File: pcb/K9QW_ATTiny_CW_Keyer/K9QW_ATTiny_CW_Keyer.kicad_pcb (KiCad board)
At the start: 2 copper layers, 50.8 x 31.8 mm, 37 parts, among them J1 Power Input, J2 AudioJack4, J3 AudioJack4, J4 Sidetone, J5 Mounting Hole, Q1 AO3401A, Q2 MMBT2222A, Q3 MMBT3904, Q4 MMBT3904, SW1 Power Switch, SW2 Command, U1 ATtiny85-20P, U2 LD1117S33TR_SOT223

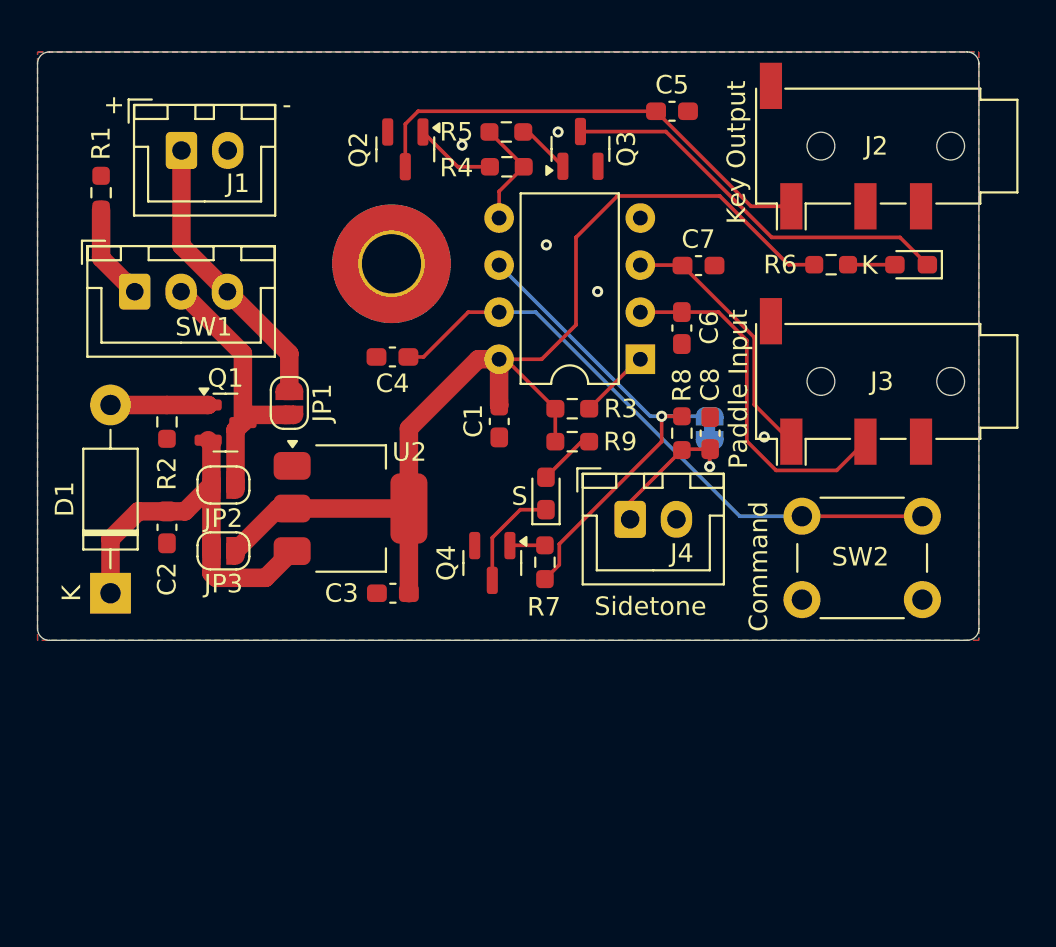
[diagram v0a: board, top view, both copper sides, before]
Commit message: Adding power supply filter cap and preparing buzzer
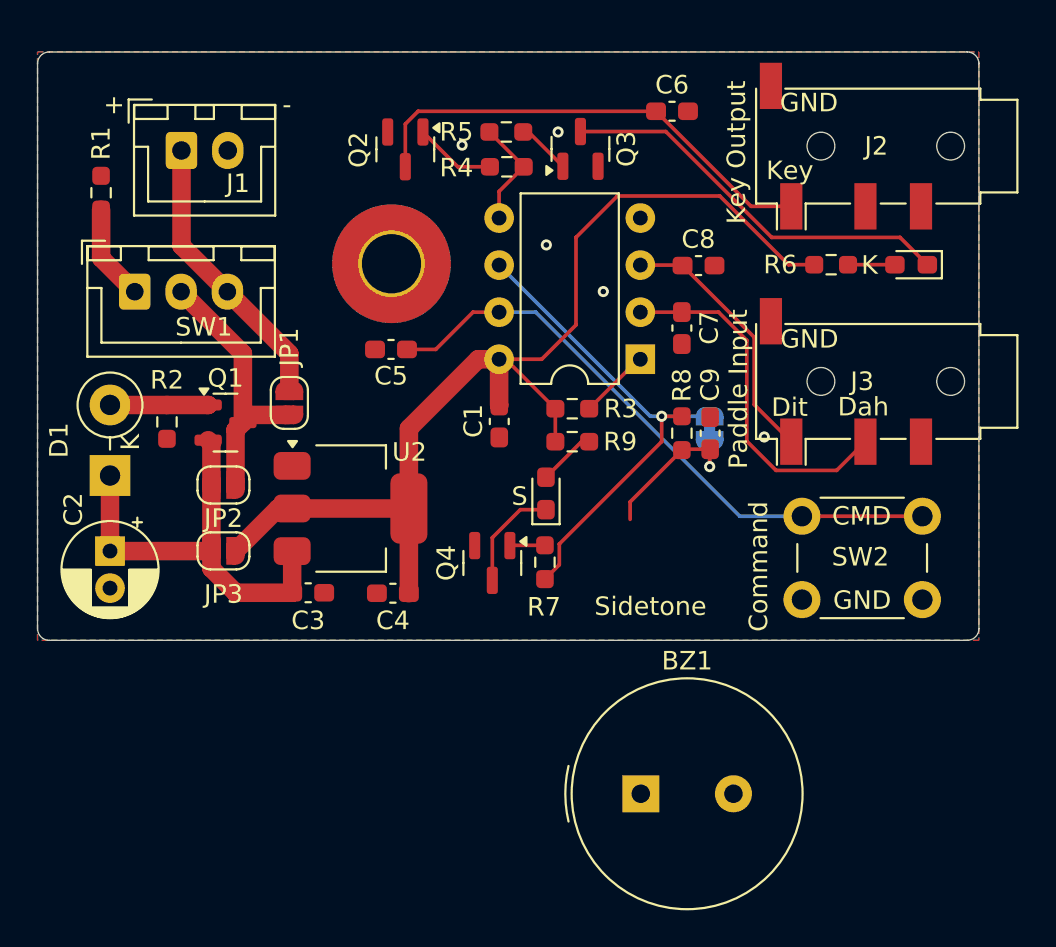
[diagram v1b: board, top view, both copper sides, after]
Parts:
- removed J4: Sidetone, Connector_JST:JST_XH_B2B-XH-A_1x02_P2.50mm_Vertical
- added BZ1: Buzzer, Buzzer_Beeper:Buzzer_TDK_PS1240P02BT_D12.2mm_H6.5mm, F.Cu at (159.0, 126.1)
- added C2: 10uF, Capacitor_THT:CP_Radial_D5.0mm_P2.00mm, F.Cu at (130.4, 113.0)
- D1: footprint Diode_THT:D_DO-41_SOD81_P10.16mm_Horizontal -> Diode_THT:D_DO-41_SOD81_P3.81mm_Vertical_KathodeUp
- D2: value Key -> Key LED
- D3: value Sidetone -> Sidetone LED
- R1: value 50 -> 1k
- R6, R9: value 220 -> 220R
- R8: value 8.2 -> 8.2R
- moved C3 8.40 mm to (141.1, 115.3), turned to 0 degrees
- moved D1 6.35 mm to (130.4, 109.0)
- moved C5 0.41 mm to (145.6, 102.2)
- renumbered C2 to C3, C3 to C4, C4 to C5, C5 to C6, C6 to C7, C7 to C8, C8 to C9
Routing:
- net Net-(D1-K): track 22.8 -> 24.6 mm
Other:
- board text added: "CMD"
- board text added: "Dah"
- board text added: "Dit"
- board text added: "GND"
- board text added: "Key"

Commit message: Laying out buzzer and moving power regulator to back of board
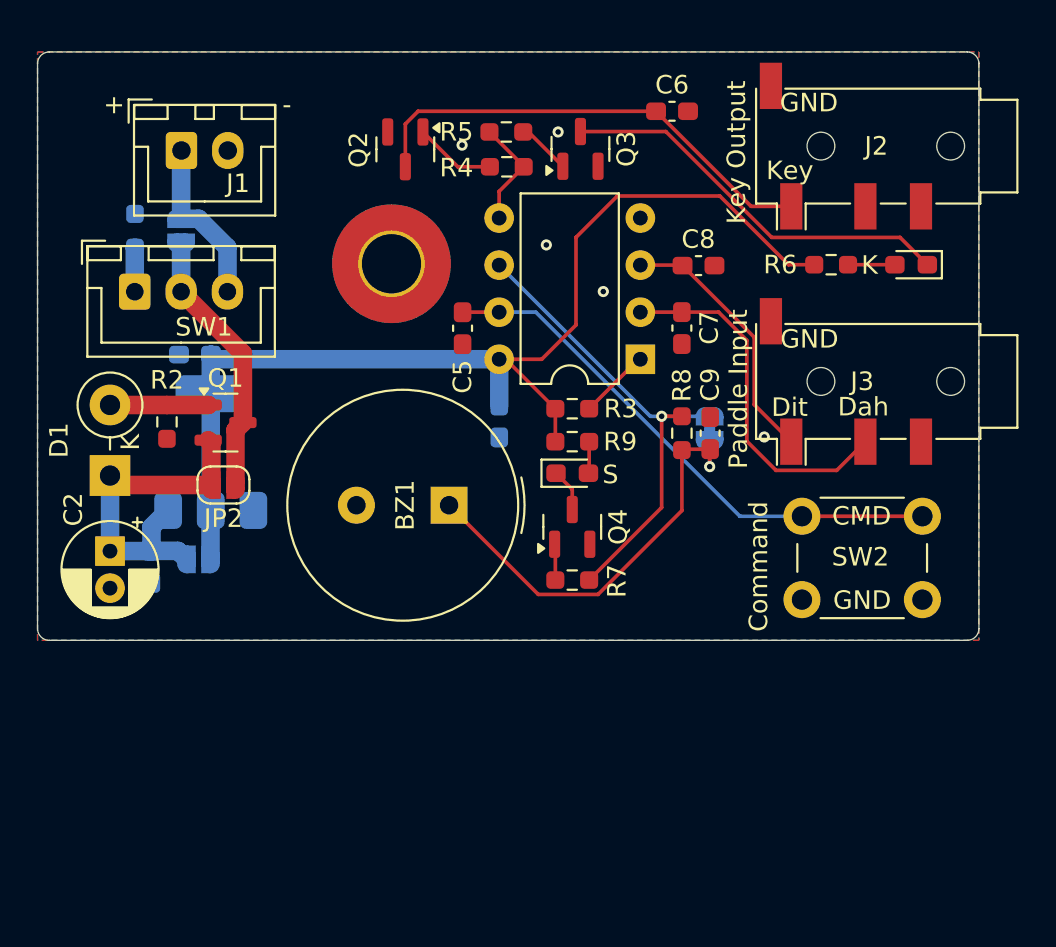
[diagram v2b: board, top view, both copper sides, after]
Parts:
- C1, C3, C4, JP1, JP3, R1, U2: moved to B.Cu
- moved BZ1 18.7 mm to (148.7, 110.6), turned to 180 degrees
- moved C4 16.7 mm to (135.0, 102.4)
- moved JP1 11.0 mm to (134.2, 95.8)
- moved C3 8.57 mm to (132.6, 113.9), turned to -90 degrees
- moved U2 8.14 mm to (135.8, 107.7), turned to 90 degrees
- moved Q4 4.73 mm to (155.3, 111.7), turned to 90 degrees
- moved C5 4.03 mm to (149.4, 101.0), turned to -90 degrees
- moved R1 2.75 mm to (131.7, 95.8)
- moved D3 1.79 mm to (155.3, 108.8), turned to 0 degrees
- moved R7 1.76 mm to (155.3, 114.6), turned to 180 degrees
- moved JP3 1.42 mm to (135.2, 113.5)
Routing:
- net Net-(BZ1-+): track 8.81 -> 23.6 mm
- net VDC: track 15.4 -> 9.22 mm
- net Net-(D1-K): track 24.6 -> 19.1 mm
- net COMMAND: track 33.2 -> 29.4 mm
- net Net-(D3-K): track 5.82 -> 2.32 mm
- net Net-(SW1-A): track 5.18 -> 2.38 mm
- net Net-(D3-A): track 3.12 -> 1.72 mm
- net VCC: track 59.2 -> 60.3 mm
- net SIDETONE: track 27.2 -> 26.3 mm
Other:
- board text removed: "Sidetone"

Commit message: Refining routing
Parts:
- JP4: moved to F.Cu
- moved C9 11.9 mm to (155.2, 115.8), turned to 0 degrees
- moved JP4 10.5 mm to (155.2, 113.7), turned to 0 degrees
- moved R8 7.83 mm to (155.2, 111.7), turned to 180 degrees
- moved Q4 6.52 mm to (161.0, 108.5), turned to 180 degrees
- moved R7 4.52 mm to (155.2, 110.1), turned to 0 degrees
- moved D3 0.35 mm to (155.2, 108.5)
- moved R9 0.24 mm to (155.2, 106.9)
- moved BZ1 0.23 mm to (148.5, 110.6)
- moved R3 0.13 mm to (155.2, 105.4)
- renumbered J5 to J4
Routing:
- net Net-(BZ1-+): track 23.6 -> 13.9 mm, vias 1 -> 0
- net Net-(Q4-B): track 1.95 -> 6.08 mm
- net Net-(D3-K): track 2.32 -> 6.37 mm
- net SIDETONE: track 26.3 -> 22.3 mm, vias 1 -> 0
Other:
- board text added: "Sidetone"

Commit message: Minor
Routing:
- net GND: vias 5 -> 6
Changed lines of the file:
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@@
 		)
 		(fp_text user "K"
-			(at 1.8 1.1 90)
+			(at 1.5748 1.016 90)
 			(layer "F.SilkS")
 			(effects
@@
 		(tags "resistor handsolder")
 		(property "Reference" "R1"
-			(at 2.667 0 90)
+			(at 0 -1.3462 90)
 			(layer "B.SilkS")
 			(effects
@@
 		(tags "solder jumper open")
 		(property "Reference" "JP1"
-			(at 3.0122 0 90)
+			(at 0 1.7526 90)
 			(layer "B.SilkS")
 			(effects
@@
 		(size 0.6)
 		(drill 0.3)
+		(layers "F.Cu" "B.Cu")
+		(free yes)
+		(net 2)
+	)
+	(via
+		(at 150.0886 104.4448)
+		(size 0.6)
+		(drill 0.3)

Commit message: Minor
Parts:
- moved BZ1 3.57 mm to (145.8, 112.9), turned to 90 degrees
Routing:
- net Net-(BZ1-+): track 13.9 -> 15.1 mm
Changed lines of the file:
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@@
 	(footprint "Buzzer_Beeper:Buzzer_TDK_PS1240P02BT_D12.2mm_H6.5mm"
 		(layer "F.Cu")
-		(at 148.471585 110.5662 180)
+		(at 145.796 112.9284 90)
 		(descr "Buzzer, D12.2mm height 6.5mm, https://product.tdk.com/info/en/catalog/datasheets/piezoelectronic_buzzer_ps_en.pdf")
 		(tags "buzzer")
 		(property "Reference" "BZ1"
-			(at 2.548585 -1.9812 180)
+			(at 2.5 0 90)
 			(layer "F.SilkS")
 			(effects
@@
 		)
 		(property "Value" "Buzzer"
-			(at 2.5 7.31 360)
+			(at 2.5 7.31 90)
 			(layer "F.Fab")
 			(effects
@@
 		)
 		(property "Footprint" "Buzzer_Beeper:Buzzer_TDK_PS1240P02BT_D12.2mm_H6.5mm"
-			(at 0 0 180)
+			(at 0 0 90)
 			(unlocked yes)
 			(layer "F.Fab")
@@
 		)
 		(property "Datasheet" ""
-			(at 0 0 180)
+			(at 0 0 90)
 			(unlocked yes)
 			(layer "F.Fab")
@@
 		)
 		(property "Description" "Buzzer, polarized"
-			(at 0 0 180)
+			(at 0 0 90)
 			(unlocked yes)
 			(layer "F.Fab")
@@
 		)
 		(fp_text user "${REFERENCE}"
-			(at 2.5 -2.43 360)
+			(at 2.5 -2.43 90)
 			(layer "F.Fab")
 			(effects
@@
 		)
 		(pad "1" thru_hole rect
-			(at 0 0 180)
+			(at 0 0 90)
 			(size 2 2)
 			(drill 1)
@@
 		)
 		(pad "2" thru_hole circle
-			(at 5 0 180)
+			(at 5 0 90)
 			(size 2 2)
 			(drill 1)
@@
 	)
 	(gr_text "Sidetone"
-		(at 141.2494 108.966 0)
+		(at 144.2466 115.2652 90)
 		(layer "F.SilkS")
 		(effects
@@
 	)
 	(segment
-		(start 149.2261 110.5662)
-		(end 148.700185 110.5662)
-		(width 0.2)
-		(layer "F.Cu")
-		(net 25)
-	)
-	(segment
 		(start 155.8694 114.3115)
 		(end 155.8694 113.7412)
@@
 	(segment
 		(start 154.3569 115.824)
-		(end 153.729385 115.824)
+		(end 148.505215 115.824)
 		(width 0.2)
 		(layer "F.Cu")
@@
 	)
 	(segment
-		(start 155.8694 111.9209)
-		(end 156.1319 111.6584)
+		(start 148.505215 115.824)
+		(end 145.7198 113.038585)
 		(width 0.2)
 		(layer "F.Cu")
@@
 	)
 	(segment
-		(start 153.729385 115.824)
-		(end 148.471585 110.5662)
+		(start 155.8694 111.9209)
+		(end 156.1319 111.6584)
 		(width 0.2)
 		(layer "F.Cu")

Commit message: Minor
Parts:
- moved C1 0.13 mm to (151.4, 105.9)
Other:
- board text added: "ATTiny85 CW Keyer - Rev 0 PCB by Edward Sandor, K9QW 2024-08"
- board text removed: "ATTiny85 CW Keyer PCB by Edward Sandor, K9QW Sandor Laboratories 2024-08 Rev 1"
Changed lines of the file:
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@@
 	(footprint "Capacitor_SMD:C_0603_1608Metric_Pad1.08x0.95mm_HandSolder"
 		(layer "B.Cu")
-		(at 151.4094 106.045 -90)
+		(at 151.4094 105.9169 -90)
 		(descr "Capacitor SMD 0603 (1608 Metric), square (rectangular) end terminal, IPC_7351 nominal with elongated pad for handsoldering. (Body size source: IPC-SM-782 page 76, https://www.pcb-3d.com/wordpress/wp-content/uploads/ipc-sm-782a_amendment_1_and_2.pdf), generated with kicad-footprint-generator")
 		(tags "capacitor handsolder")
 		(property "Reference" "C1"
-			(at 0 -1.5748 90)
+			(at 2.5908 -0.0254 90)
 			(layer "B.SilkS")
 			(effects
@@
 		(layer "Edge.Cuts")
 	)
-	(gr_text "ATTiny85 CW Keyer\nPCB by Edward Sandor, K9QW\nSandor Laboratories\n2024-08 Rev 1"
-		(at 150.5458 109.6772 180)
+	(gr_text "ATTiny85 CW Keyer - Rev 0\nPCB by Edward Sandor, K9QW\n2024-08"
+		(at 166.5478 92.5322 0)
 		(layer "B.SilkS")
 		(effects
@@
 	)
 	(gr_text "github.com/ewsandor/ATTiny85_CW_Keyer"
-		(at 145.1102 87.0712 180)
+		(at 166.0906 116.1034 0)
 		(layer "B.SilkS")
 		(effects
@@
 		(width 0.2)
 		(layer "F.Cu")
+		(net 1)
+	)
+	(segment
+		(start 151.4094 102.6968)
+		(end 151.401 102.6884)
+		(width 1)
+		(layer "B.Cu")
 		(net 1)
 	)
@@
 	)
 	(segment
-		(start 151.4094 105.1825)
+		(start 151.4094 105.0544)
 		(end 151.4094 102.6968)
 		(width 1)
@@
 		(start 151.401 102.6884)
 		(end 136.1011 102.6884)
-		(width 1)
-		(layer "B.Cu")
-		(net 1)
-	)
-	(segment
-		(start 151.4094 102.6968)
-		(end 151.401 102.6884)
 		(width 1)
 		(layer "B.Cu")
@@
 	)
 	(via
+		(at 152.8826 106.172)
+		(size 0.6)
+		(drill 0.3)
+		(layers "F.Cu" "B.Cu")
+		(free yes)
+		(net 2)
+	)
+	(via
 		(at 149.4028 91.1352)
 		(size 0.6)
@@
 		(size 0.6)
 		(drill 0.3)
-		(layers "F.Cu" "B.Cu")
-		(free yes)
-		(net 2)
-	)
-	(via
-		(at 150.0886 104.4448)
-		(size 0.6)
-		(drill 0.3)
